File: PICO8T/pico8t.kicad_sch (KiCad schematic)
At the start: 97 parts, among them J0 Conn_01x16

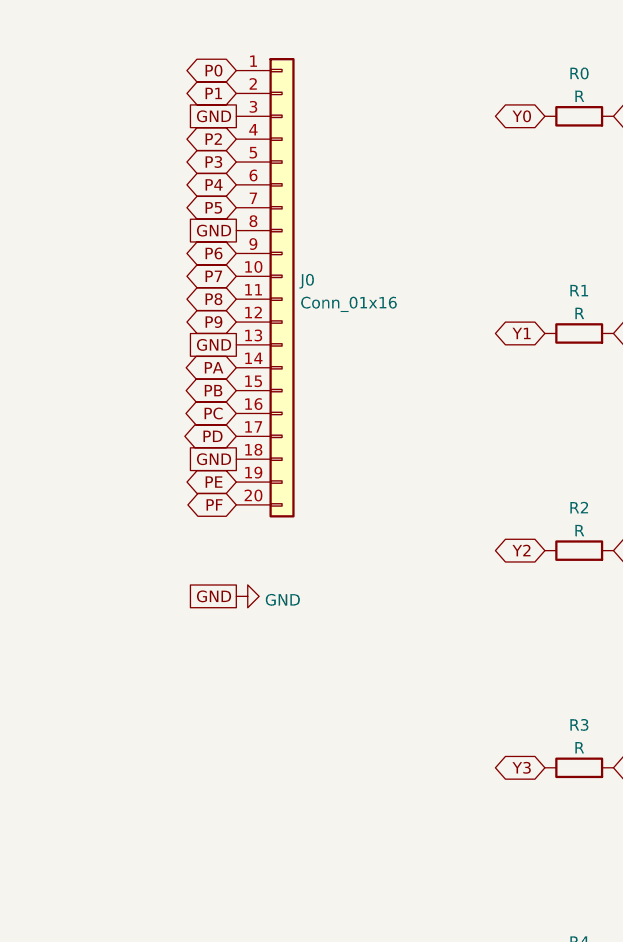
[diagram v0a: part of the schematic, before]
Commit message: Matrix8T revision with first driver
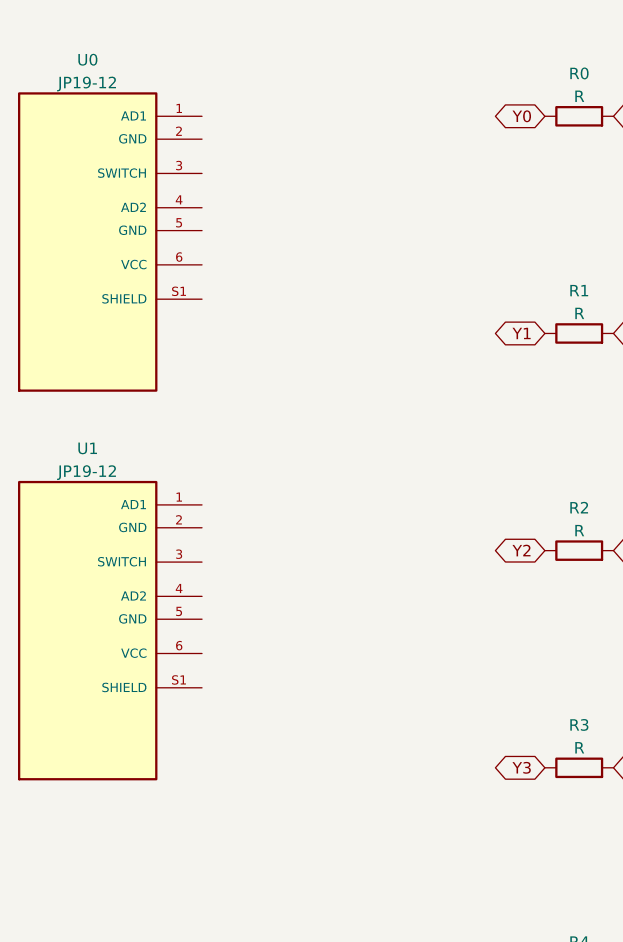
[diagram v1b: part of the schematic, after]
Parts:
- removed J0: Conn_01x16, Connector_PinHeader_2.54mm:PinHeader_1x20_P2.54mm_Vertical, symbol Connector_Generic:Conn_01x20
- added U0, U1: JP19-12, Library:JP19-012, symbol Analog Stick:JP19-12
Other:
- title: PICO8T -> pico8t
